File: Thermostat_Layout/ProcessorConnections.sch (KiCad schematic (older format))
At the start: 15 parts, among them J1 Conn_01x03, SW1 SW_Push, U1 LM50CIM3, U2 ATMEGA328P-AU, U7 FM25V10, Y1 Crystal

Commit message: Update schematic
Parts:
- renumbered C2 to C1, C3 to C2, C1 to C3, R13 to R3, R3 to R4, R4 to R5, U7 to U2, U2 to U3
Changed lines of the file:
@@
 $EndDescr
 $Comp
-L dk_Embedded-Microcontrollers:ATMEGA328P-AU U2
+L dk_Embedded-Microcontrollers:ATMEGA328P-AU U3
 U 1 1 5D3DFFF8
 P 6300 2950
-F 0 "U2" H 6628 3053 60  0000 L CNN
+F 0 "U3" H 6628 3053 60  0000 L CNN
 F 1 "ATMEGA328P-AU" H 6628 2947 60  0000 L CNN
 F 2 "digikey-footprints:TQFP-32_7x7mm" H 6500 3150 60  0001 L CNN
@@
 Connection ~ 6400 4450
 $Comp
-L SparkFun-PowerSymbols:GND #GND0101
+L SparkFun-PowerSymbols:GND #GND05
 U 1 1 5D3E1674
 P 6400 4450
-F 0 "#GND0101" H 6450 4400 45  0001 L BNN
+F 0 "#GND05" H 6450 4400 45  0001 L BNN
 F 1 "GND" H 6400 4280 45  0000 C CNN
 F 2 "" H 6400 4350 60  0001 C CNN
@@
 Connection ~ 6400 1350
 $Comp
-L SparkFun-PowerSymbols:3.3V #SUPPLY0101
+L SparkFun-PowerSymbols:3.3V #SUPPLY04
 U 1 1 5D3E1EE5
 P 6400 1250
-F 0 "#SUPPLY0101" H 6450 1250 45  0001 L BNN
+F 0 "#SUPPLY04" H 6450 1250 45  0001 L BNN
 F 1 "3.3V" H 6400 1526 45  0000 C CNN
 F 2 "XXX-00000" H 6400 1431 60  0000 C CNN
@@
 	6400 1250 6400 1350
 $Comp
-L Device:C C1
+L Device:C C3
 U 1 1 5D3E2A64
 P 5200 4250
-F 0 "C1" H 5315 4296 50  0000 L CNN
+F 0 "C3" H 5315 4296 50  0000 L CNN
 F 1 "100nF" H 5315 4205 50  0000 L CNN
 F 2 "Capacitor_SMD:C_0402_1005Metric" H 5238 4100 50  0001 C CNN
@@
 $EndComp
 $Comp
-L SparkFun-PowerSymbols:GND #GND0102
+L SparkFun-PowerSymbols:GND #GND04
 U 1 1 5D3E37E7
 P 5200 4400
-F 0 "#GND0102" H 5250 4350 45  0001 L BNN
+F 0 "#GND04" H 5250 4350 45  0001 L BNN
 F 1 "GND" H 5200 4230 45  0000 C CNN
 F 2 "" H 5200 4300 60  0001 C CNN
@@
 	1950 1500 1550 1500
 $Comp
-L SparkFun-PowerSymbols:3.3V #SUPPLY0103
+L SparkFun-PowerSymbols:3.3V #SUPPLY02
 U 1 1 5D432D22
 P 2150 1200
-F 0 "#SUPPLY0103" H 2200 1200 45  0001 L BNN
+F 0 "#SUPPLY02" H 2200 1200 45  0001 L BNN
 F 1 "3.3V" H 2150 1476 45  0000 C CNN
 F 2 "XXX-00000" H 2150 1381 60  0000 C CNN
@@
 	1800 3100 2200 3100
 $Comp
-L SparkFun-PowerSymbols:GND #GND0106
+L SparkFun-PowerSymbols:GND #GND02
 U 1 1 5D47A3DC
 P 1800 3100
-F 0 "#GND0106" H 1850 3050 45  0001 L BNN
+F 0 "#GND02" H 1850 3050 45  0001 L BNN
 F 1 "GND" H 1800 2930 45  0000 C CNN
 F 2 "" H 1800 3000 60  0001 C CNN
@@
 $EndComp
 $Comp
-L SparkFun-PowerSymbols:GND #GND0107
+L SparkFun-PowerSymbols:GND #GND01
 U 1 1 5D48DCED
 P 1400 4350
-F 0 "#GND0107" H 1450 4300 45  0001 L BNN
+F 0 "#GND01" H 1450 4300 45  0001 L BNN
 F 1 "GND" H 1400 4180 45  0000 C CNN
 F 2 "" H 1400 4250 60  0001 C CNN
@@
 $EndComp
 $Comp
-L SparkFun-PowerSymbols:3.3V #SUPPLY0104
+L SparkFun-PowerSymbols:3.3V #SUPPLY01
 U 1 1 5D48E2F2
 P 1400 4150
-F 0 "#SUPPLY0104" H 1450 4150 45  0001 L BNN
+F 0 "#SUPPLY01" H 1450 4150 45  0001 L BNN
 F 1 "3.3V" H 1400 4426 45  0000 C CNN
 F 2 "XXX-00000" H 1400 4331 60  0000 C CNN
@@
 BATT_MON
 $Comp
-L FM25V10:FM25V10 U7
+L FM25V10:FM25V10 U2
 U 1 1 5D493642
 P 4000 5850
-F 0 "U7" H 4000 6481 50  0000 C CNN
+F 0 "U2" H 4000 6481 50  0000 C CNN
 F 1 "FM25V10" H 4000 6390 50  0000 C CNN
 F 2 "FM25V10:SOIC127P601X172-8N" H 4000 6550 50  0001 C CNN
@@
 Connection ~ 4700 5700
 $Comp
-L SparkFun-PowerSymbols:3.3V #SUPPLY0110
+L SparkFun-PowerSymbols:3.3V #SUPPLY03
 U 1 1 5D496E24
 P 4700 5400
-F 0 "#SUPPLY0110" H 4750 5400 45  0001 L BNN
+F 0 "#SUPPLY03" H 4750 5400 45  0001 L BNN
 F 1 "3.3V" H 4700 5676 45  0000 C CNN
 F 2 "XXX-00000" H 4700 5581 60  0000 C CNN
@@
 Connection ~ 4700 5400
 $Comp
-L SparkFun-PowerSymbols:GND #GND0117
+L SparkFun-PowerSymbols:GND #GND03
 U 1 1 5D497357
 P 4000 6400
-F 0 "#GND0117" H 4050 6350 45  0001 L BNN
+F 0 "#GND03" H 4050 6350 45  0001 L BNN
 F 1 "GND" H 4000 6230 45  0000 C CNN
 F 2 "" H 4000 6300 60  0001 C CNN
@@
 $EndComp
 $Comp
-L SparkFun-PowerSymbols:GND #GND0105
+L SparkFun-PowerSymbols:GND #GND07
 U 1 1 5D4748F4
 P 9050 1850
-F 0 "#GND0105" H 9100 1800 45  0001 L BNN
+F 0 "#GND07" H 9100 1800 45  0001 L BNN
 F 1 "GND" H 9050 1680 45  0000 C CNN
 F 2 "" H 9050 1750 60  0001 C CNN
@@
 	9200 1500 8800 1500
 $Comp
-L Device:R_US R3
+L Device:R_US R4
 U 1 1 5D475940
 P 8650 1500
-F 0 "R3" V 8445 1500 50  0000 C CNN
+F 0 "R4" V 8445 1500 50  0000 C CNN
 F 1 "1kΩ" V 8536 1500 50  0000 C CNN
 F 2 "Resistor_SMD:R_0402_1005Metric" V 8690 1490 50  0001 C CNN
@@
 $EndComp
 $Comp
-L Device:R_US R4
+L Device:R_US R5
 U 1 1 5D4760EE
 P 8650 1700
-F 0 "R4" V 8445 1700 50  0000 C CNN
+F 0 "R5" V 8445 1700 50  0000 C CNN
 F 1 "1kΩ" V 8536 1700 50  0000 C CNN
 F 2 "Resistor_SMD:R_0402_1005Metric" V 8690 1690 50  0001 C CNN
@@
 UC_RST
 $Comp
-L SparkFun-PowerSymbols:GND #GND0123
+L SparkFun-PowerSymbols:GND #GND06
 U 1 1 5D527C49
 P 8500 5000
-F 0 "#GND0123" H 8550 4950 45  0001 L BNN
+F 0 "#GND06" H 8550 4950 45  0001 L BNN
 F 1 "GND" H 8500 4830 45  0000 C CNN
 F 2 "" H 8500 4900 60  0001 C CNN
@@
 $EndComp
 $Comp
-L Device:R_US R13
+L Device:R_US R3
 U 1 1 5D52827F
 P 7800 4850
-F 0 "R13" H 7868 4896 50  0000 L CNN
+F 0 "R3" H 7868 4896 50  0000 L CNN
 F 1 "10kΩ" H 7868 4805 50  0000 L CNN
 F 2 "Resistor_SMD:R_0402_1005Metric" V 7840 4840 50  0001 C CNN
@@
 	7800 5000 7500 5000
 $Comp
-L SparkFun-PowerSymbols:3.3V #SUPPLY0111
+L SparkFun-PowerSymbols:3.3V #SUPPLY05
 U 1 1 5D528D3B
 P 7800 4700
-F 0 "#SUPPLY0111" H 7850 4700 45  0001 L BNN
+F 0 "#SUPPLY05" H 7850 4700 45  0001 L BNN
 F 1 "3.3V" H 7800 4976 45  0000 C CNN
 F 2 "XXX-00000" H 7800 4881 60  0000 C CNN
@@
 	1850 2650 1800 2650
 $Comp
-L Device:C C3
+L Device:C C2
 U 1 1 5D477AC7
 P 2200 2950
-F 0 "C3" H 2315 2996 50  0000 L CNN
+F 0 "C2" H 2315 2996 50  0000 L CNN
 F 1 "22pF" H 2315 2905 50  0000 L CNN
 F 2 "Capacitor_SMD:C_0402_1005Metric" H 2238 2800 50  0001 C CNN
@@
 $EndComp
 $Comp
-L Device:C C2
+L Device:C C1
 U 1 1 5D4774F7
 P 1800 2950
-F 0 "C2" H 1915 2996 50  0000 L CNN
+F 0 "C1" H 1915 2996 50  0000 L CNN
 F 1 "22pF" H 1915 2905 50  0000 L CNN
 F 2 "Capacitor_SMD:C_0402_1005Metric" H 1838 2800 50  0001 C CNN

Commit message: Layout changes
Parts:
- removed U2: FM25V10, FM25V10:SOIC127P601X172-8N, symbol FM25V10:FM25V10
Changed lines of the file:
@@
 BATT_MON
-$Comp
-L FM25V10:FM25V10 U2
-U 1 1 5D493642
-P 4000 5850
-F 0 "U2" H 4000 6481 50  0000 C CNN
-F 1 "FM25V10" H 4000 6390 50  0000 C CNN
-F 2 "FM25V10:SOIC127P601X172-8N" H 4000 6550 50  0001 C CNN
-F 3 "" H 4000 5850 50  0001 C CNN
-	1    4000 5850
-	1    0    0    -1
-$EndComp
-Wire Wire Line
-	4500 5700 4700 5700
-Wire Wire Line
-	4700 5700 4700 6000
-Wire Wire Line
-	4700 6000 4500 6000
-Wire Wire Line
-	4000 5400 4700 5400
-Wire Wire Line
-	4700 5400 4700 5700
-Connection ~ 4700 5700
-$Comp
-L SparkFun-PowerSymbols:3.3V #SUPPLY03
-U 1 1 5D496E24
-P 4700 5400
-F 0 "#SUPPLY03" H 4750 5400 45  0001 L BNN
-F 1 "3.3V" H 4700 5676 45  0000 C CNN
-F 2 "XXX-00000" H 4700 5581 60  0000 C CNN
-F 3 "" H 4700 5400 60  0001 C CNN
-	1    4700 5400
-	1    0    0    -1
-$EndComp
-Connection ~ 4700 5400
-$Comp
-L SparkFun-PowerSymbols:GND #GND03
-U 1 1 5D497357
-P 4000 6400
-F 0 "#GND03" H 4050 6350 45  0001 L BNN
-F 1 "GND" H 4000 6230 45  0000 C CNN
-F 2 "" H 4000 6300 60  0001 C CNN
-F 3 "" H 4000 6300 60  0001 C CNN
-	1    4000 6400
-	1    0    0    -1
-$EndComp
-Wire Wire Line
-	3500 5700 3000 5700
-Wire Wire Line
-	3500 5850 3000 5850
-Wire Wire Line
-	3500 6000 3000 6000
-Wire Wire Line
-	3500 6150 3000 6150
-Text GLabel 3000 5700 0    50   Input ~ 0
-MEM_CS
-Text GLabel 3000 5850 0    50   Output ~ 0
-MISO
-Text GLabel 3000 6000 0    50   Input ~ 0
-MOSI
-Text GLabel 3000 6150 0    50   Input ~ 0
-SCK
 $Comp
 L Connector_Generic:Conn_01x03 J1

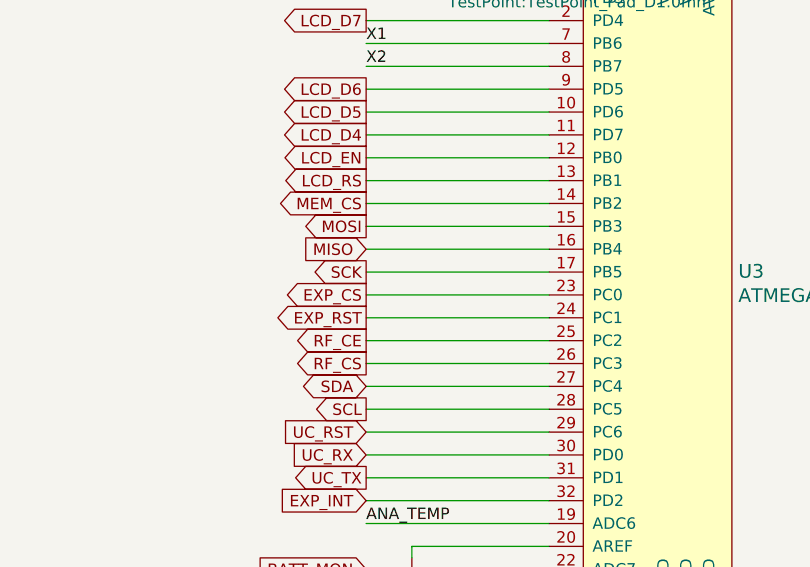
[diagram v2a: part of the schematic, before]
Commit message: Swap out the MCP23s17 for the MCP23017
Removes the need for the SPI bus
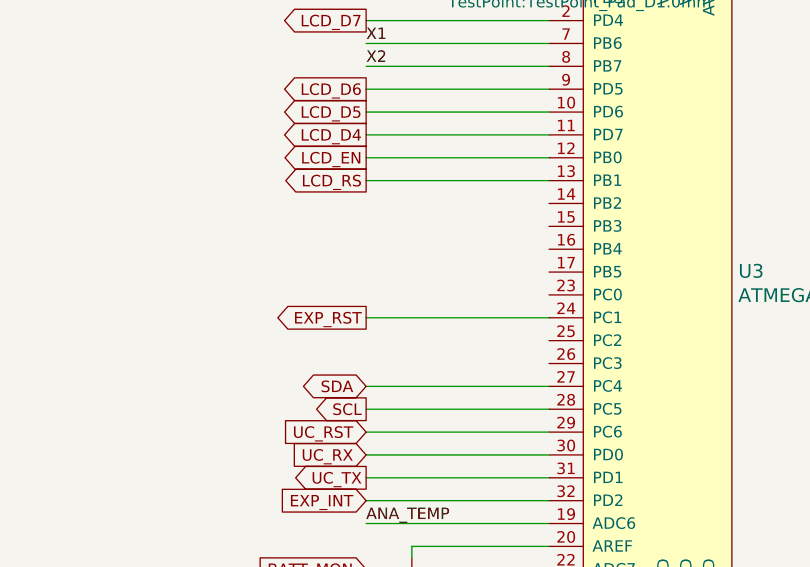
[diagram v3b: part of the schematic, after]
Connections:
- net EXP_CS: no longer names the net of U3.23 (PC0)
- net MEM_CS: no longer names the net of U3.14 (PB2)
- net MISO: no longer names the net of U3.16 (PB4)
- net MOSI: no longer names the net of U3.15 (PB3)
- net RF_CE: no longer names the net of U3.25 (PC2)
- net RF_CS: no longer names the net of U3.26 (PC3)
- net SCK: no longer names the net of U3.17 (PB5)
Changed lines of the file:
@@
 LCD_RS
 Wire Wire Line
-	5800 2550 5000 2550
-Text GLabel 5000 2550 0    50   Output ~ 0
-MEM_CS
-Wire Wire Line
-	5800 2650 5000 2650
-Wire Wire Line
-	5800 2750 5000 2750
-Wire Wire Line
-	5800 2850 5000 2850
-Text GLabel 5000 2650 0    50   Output ~ 0
-MOSI
-Text GLabel 5000 2750 0    50   Input ~ 0
-MISO
-Text GLabel 5000 2850 0    50   Output ~ 0
-SCK
-Wire Wire Line
-	5800 2950 5000 2950
-Wire Wire Line
 	5800 3050 5000 3050
-Text GLabel 5000 2950 0    50   Output ~ 0
-EXP_CS
 Text GLabel 5000 3050 0    50   Output ~ 0
 EXP_RST
 Wire Wire Line
-	5800 3150 5000 3150
-Wire Wire Line
-	5800 3250 5000 3250
-Text GLabel 5000 3150 0    50   Output ~ 0
-RF_CE
-Text GLabel 5000 3250 0    50   Output ~ 0
-RF_CS
-Wire Wire Line
 	5800 3350 5000 3350

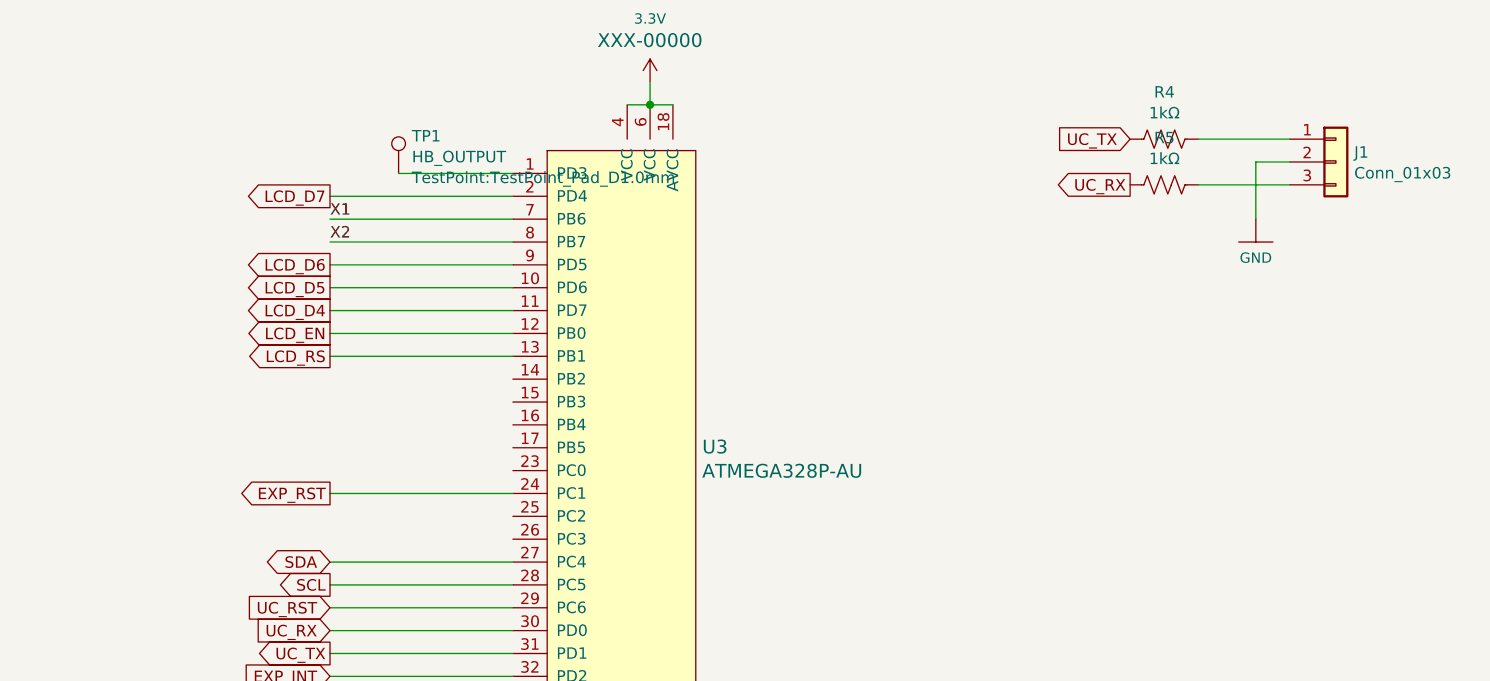
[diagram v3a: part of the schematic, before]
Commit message: FInalize schematic for thermostat
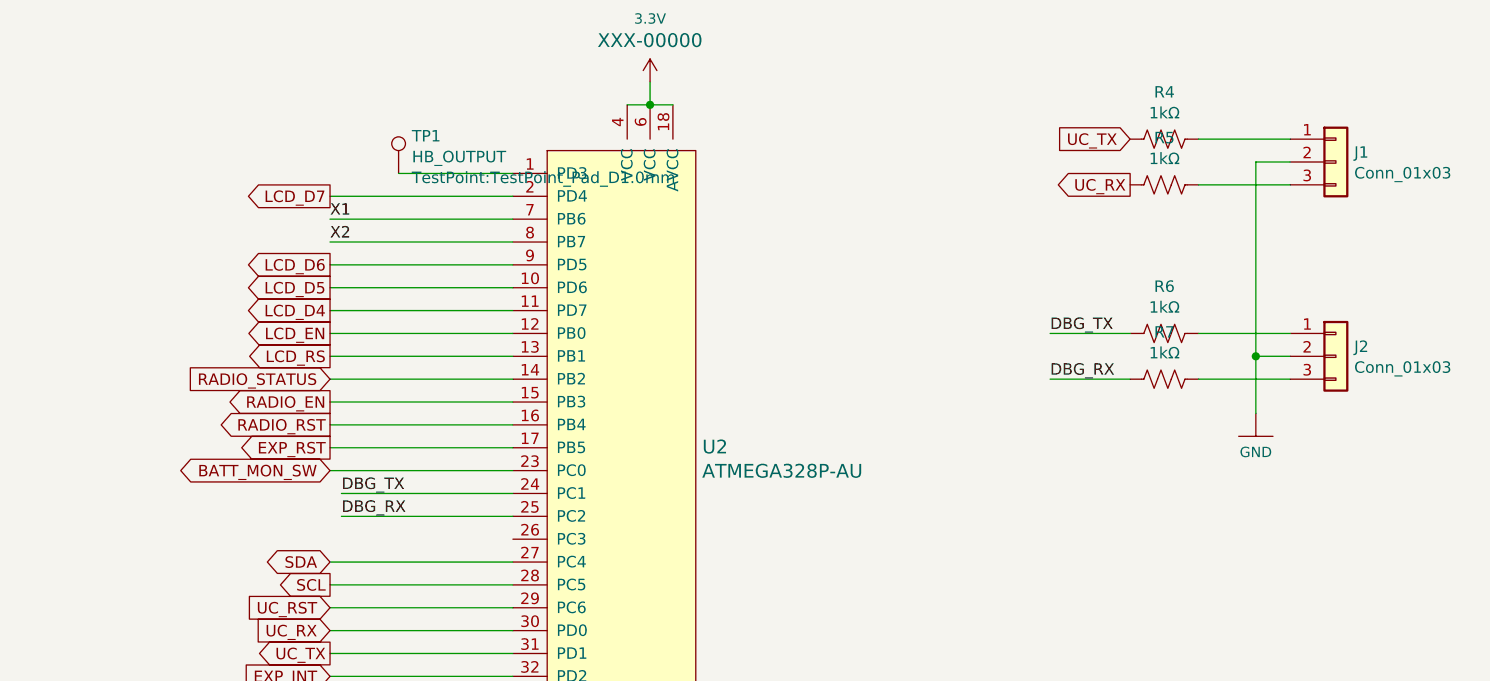
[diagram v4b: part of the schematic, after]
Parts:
- added J2: Conn_01x03, Connector_JST:JST_PH_S3B-PH-SM4-TB_1x03-1MP_P2.00mm_Horizontal, symbol Connector_Generic:Conn_01x03
- added R6, R7: 1kΩ, Resistor_SMD:R_0402_1005Metric, symbol Device:R_US
- renumbered U3 to U2
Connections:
- net EXP_RST: now also U2.17 (PB5); no longer U2.24 (PC1)
- net GND: now also J2.2 (Pin_2)
- net RADIO_STATUS: now reaches U2.14 (PB2)
- net RADIO_EN: now reaches U2.15 (PB3)
- net RADIO_RST: now reaches U2.16 (PB4)
- net BATT_MON_SW: now reaches U2.23 (PC0)
- net DBG_RX: now reaches U2.25 (PC2)
- net DBG_RX: now also R7.2
- new net: J2.1 (Pin_1), R6.1
- new net: J2.3 (Pin_3), R7.1
- new net DBG_TX: R6.2, U2.24 (PC1)
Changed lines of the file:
@@
 $EndDescr
 $Comp
-L dk_Embedded-Microcontrollers:ATMEGA328P-AU U3
+L dk_Embedded-Microcontrollers:ATMEGA328P-AU U2
 U 1 1 5D3DFFF8
 P 6300 2950
-F 0 "U3" H 6628 3053 60  0000 L CNN
+F 0 "U2" H 6628 3053 60  0000 L CNN
 F 1 "ATMEGA328P-AU" H 6628 2947 60  0000 L CNN
 F 2 "digikey-footprints:TQFP-32_7x7mm" H 6500 3150 60  0001 L CNN
@@
 Connection ~ 6400 4450
 $Comp
-L SparkFun-PowerSymbols:GND #GND05
+L SparkFun-PowerSymbols:GND #GND04
 U 1 1 5D3E1674
 P 6400 4450
-F 0 "#GND05" H 6450 4400 45  0001 L BNN
+F 0 "#GND04" H 6450 4400 45  0001 L BNN
 F 1 "GND" H 6400 4280 45  0000 C CNN
 F 2 "" H 6400 4350 60  0001 C CNN
@@
 Connection ~ 6400 1350
 $Comp
-L SparkFun-PowerSymbols:3.3V #SUPPLY04
+L SparkFun-PowerSymbols:3.3V #SUPPLY03
 U 1 1 5D3E1EE5
 P 6400 1250
-F 0 "#SUPPLY04" H 6450 1250 45  0001 L BNN
+F 0 "#SUPPLY03" H 6450 1250 45  0001 L BNN
 F 1 "3.3V" H 6400 1526 45  0000 C CNN
 F 2 "XXX-00000" H 6400 1431 60  0000 C CNN
@@
 $EndComp
 $Comp
-L SparkFun-PowerSymbols:GND #GND04
+L SparkFun-PowerSymbols:GND #GND03
 U 1 1 5D3E37E7
 P 5200 4400
-F 0 "#GND04" H 5250 4350 45  0001 L BNN
+F 0 "#GND03" H 5250 4350 45  0001 L BNN
 F 1 "GND" H 5200 4230 45  0000 C CNN
 F 2 "" H 5200 4300 60  0001 C CNN
@@
 Text GLabel 5000 2450 0    50   Output ~ 0
 LCD_RS
-Wire Wire Line
-	5800 3050 5000 3050
-Text GLabel 5000 3050 0    50   Output ~ 0
-EXP_RST
 Wire Wire Line
 	5800 3350 5000 3350
@@
 	1    0    0    -1
 $EndComp
-$Comp
-L SparkFun-PowerSymbols:GND #GND07
-U 1 1 5D4748F4
-P 9050 1850
-F 0 "#GND07" H 9100 1800 45  0001 L BNN
-F 1 "GND" H 9050 1680 45  0000 C CNN
-F 2 "" H 9050 1750 60  0001 C CNN
-F 3 "" H 9050 1750 60  0001 C CNN
-	1    9050 1850
-	1    0    0    -1
-$EndComp
 Wire Wire Line
 	9200 1600 9050 1600
-Wire Wire Line
-	9050 1600 9050 1850
 Wire Wire Line
 	8800 1700 9200 1700
@@
 UC_RST
 $Comp
-L SparkFun-PowerSymbols:GND #GND06
+L SparkFun-PowerSymbols:GND #GND05
 U 1 1 5D527C49
 P 8500 5000
-F 0 "#GND06" H 8550 4950 45  0001 L BNN
+F 0 "#GND05" H 8550 4950 45  0001 L BNN
 F 1 "GND" H 8500 4830 45  0000 C CNN
 F 2 "" H 8500 4900 60  0001 C CNN
@@
 	7800 5000 7500 5000
 $Comp
-L SparkFun-PowerSymbols:3.3V #SUPPLY05
+L SparkFun-PowerSymbols:3.3V #SUPPLY04
 U 1 1 5D528D3B
 P 7800 4700
-F 0 "#SUPPLY05" H 7850 4700 45  0001 L BNN
+F 0 "#SUPPLY04" H 7850 4700 45  0001 L BNN
 F 1 "3.3V" H 7800 4976 45  0000 C CNN
 F 2 "XXX-00000" H 7800 4881 60  0000 C CNN
@@
 	1    0    0    -1
 $EndComp
+Text GLabel 5000 2550 0    50   Input ~ 0
+RADIO_STATUS
+Wire Wire Line
+	5000 2550 5800 2550
+Text GLabel 5000 2650 0    50   Output ~ 0
+RADIO_EN
+Text GLabel 5000 2750 0    50   Output ~ 0
+RADIO_RST
+Wire Wire Line
+	5000 2650 5800 2650
+Wire Wire Line
+	5000 2750 5800 2750
+Text GLabel 5000 2850 0    50   Output ~ 0
+EXP_RST
+Wire Wire Line
+	5000 2850 5800 2850
+Text GLabel 5000 2950 0    50   3State ~ 0
+BATT_MON_SW
+Wire Wire Line
+	5000 2950 5800 2950
+Text Label 5050 3050 0    50   ~ 0
+DBG_TX
+Text Label 5050 3150 0    50   ~ 0
+DBG_RX
+Wire Wire Line
+	5800 3050 5050 3050
+Wire Wire Line
+	5050 3150 5800 3150
+$Comp
+L Connector_Generic:Conn_01x03 J2
+U 1 1 5DA149FD
+P 9400 2450
+F 0 "J2" H 9480 2492 50  0000 L CNN
+F 1 "Conn_01x03" H 9480 2401 50  0000 L CNN
+F 2 "Connector_JST:JST_PH_S3B-PH-SM4-TB_1x03-1MP_P2.00mm_Horizontal" H 9400 2450 50  0001 C CNN
+F 3 "~" H 9400 2450 50  0001 C CNN
+	1    9400 2450
+	1    0    0    -1
+$EndComp
+$Comp
+L SparkFun-PowerSymbols:GND #GND06
+U 1 1 5DA14A03
+P 9050 2700
+F 0 "#GND06" H 9100 2650 45  0001 L BNN
+F 1 "GND" H 9050 2530 45  0000 C CNN
+F 2 "" H 9050 2600 60  0001 C CNN
+F 3 "" H 9050 2600 60  0001 C CNN
+	1    9050 2700
+	1    0    0    -1
+$EndComp
+Wire Wire Line
+	9200 2450 9050 2450
+Wire Wire Line
+	9050 2450 9050 2700
+Wire Wire Line
+	8800 2550 9200 2550
+Wire Wire Line
+	9200 2350 8800 2350
+$Comp
+L Device:R_US R6
+U 1 1 5DA14A0D
+P 8650 2350
+F 0 "R6" V 8445 2350 50  0000 C CNN
+F 1 "1kΩ" V 8536 2350 50  0000 C CNN
+F 2 "Resistor_SMD:R_0402_1005Metric" V 8690 2340 50  0001 C CNN
+F 3 "~" H 8650 2350 50  0001 C CNN
+	1    8650 2350
+	0    1    1    0
+$EndComp
+$Comp
+L Device:R_US R7
+U 1 1 5DA14A13
+P 8650 2550
+F 0 "R7" V 8445 2550 50  0000 C CNN
+F 1 "1kΩ" V 8536 2550 50  0000 C CNN
+F 2 "Resistor_SMD:R_0402_1005Metric" V 8690 2540 50  0001 C CNN
+F 3 "~" H 8650 2550 50  0001 C CNN
+	1    8650 2550
+	0    1    1    0
+$EndComp
+Wire Wire Line
+	9050 1600 9050 2450
+Connection ~ 9050 2450
+Wire Wire Line
+	8500 2350 8150 2350
+Wire Wire Line
+	8500 2550 8150 2550
+Text Label 8150 2350 0    50   ~ 0
+DBG_TX
+Text Label 8150 2550 0    50   ~ 0
+DBG_RX
 $EndSCHEMATC
